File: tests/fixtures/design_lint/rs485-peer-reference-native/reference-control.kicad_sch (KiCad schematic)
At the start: 4 parts, among them J1 Synthetic RS-485 endpoint, J2 Synthetic RS-485 endpoint, J3 Synthetic RS-485 endpoint, U1 Synthetic RS-485 transceiver

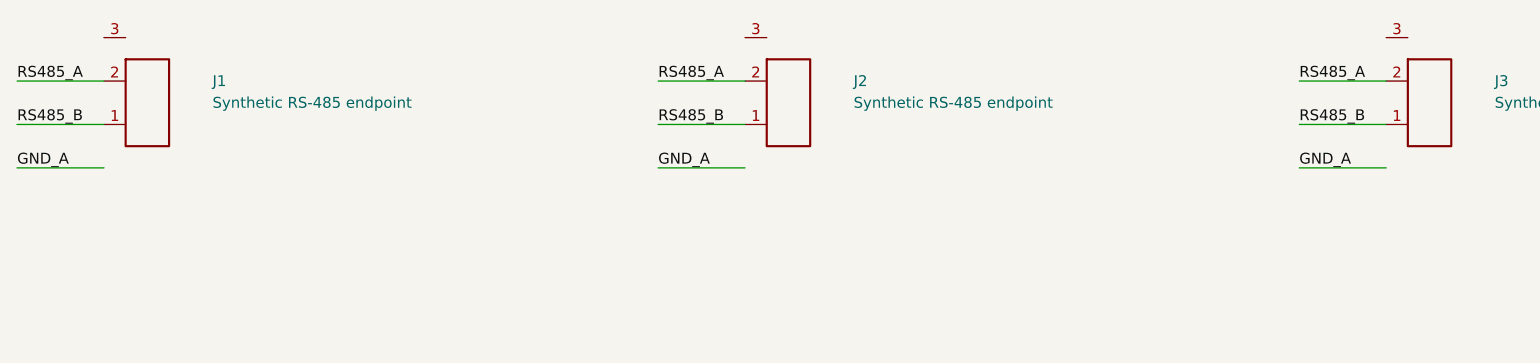
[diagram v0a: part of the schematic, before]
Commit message: Fix RS-485 native fixture gate
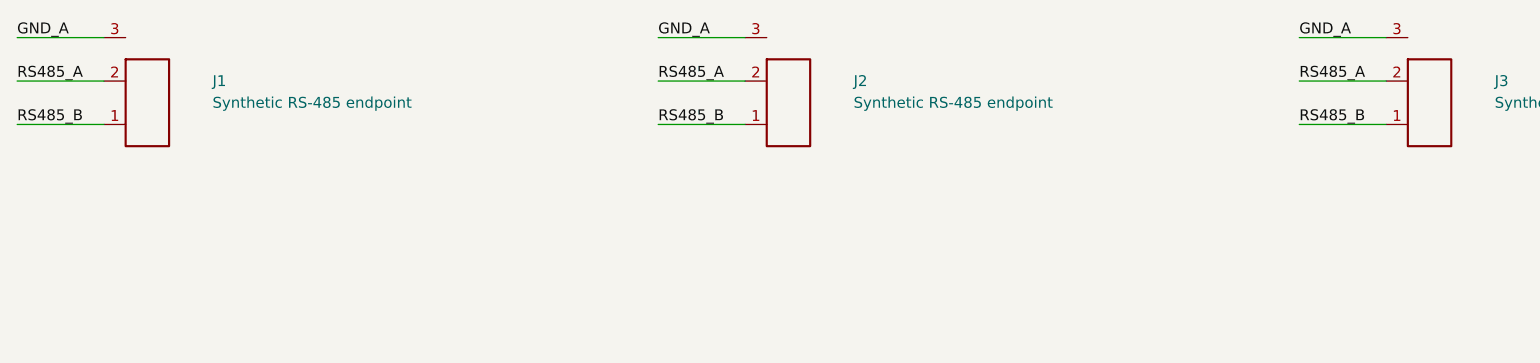
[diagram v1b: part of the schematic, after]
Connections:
- net GND_A: now also J1.3 (REF), J2.3 (REF), J3.3 (REF)
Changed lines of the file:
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@@
     (effects (font (size 1.27 1.27)) (justify left bottom))
 )
-  (wire (pts (xy 59.92 77.62) (xy 49.76 77.62))
+  (wire (pts (xy 59.92 62.38) (xy 49.76 62.38))
     (stroke (width 0) (type default))
 )
-  (label "GND_A" (at 49.76 77.62 0)
+  (label "GND_A" (at 49.76 62.38 0)
     (effects (font (size 1.27 1.27)) (justify left bottom))
 )
@@
     (effects (font (size 1.27 1.27)) (justify left bottom))
 )
-  (wire (pts (xy 134.92 77.62) (xy 124.76 77.62))
+  (wire (pts (xy 134.92 62.38) (xy 124.76 62.38))
     (stroke (width 0) (type default))
 )
-  (label "GND_A" (at 124.76 77.62 0)
+  (label "GND_A" (at 124.76 62.38 0)
     (effects (font (size 1.27 1.27)) (justify left bottom))
 )
@@
     (effects (font (size 1.27 1.27)) (justify left bottom))
 )
-  (wire (pts (xy 209.92 77.62) (xy 199.76 77.62))
+  (wire (pts (xy 209.92 62.38) (xy 199.76 62.38))
     (stroke (width 0) (type default))
 )
-  (label "GND_A" (at 199.76 77.62 0)
+  (label "GND_A" (at 199.76 62.38 0)
     (effects (font (size 1.27 1.27)) (justify left bottom))
 )

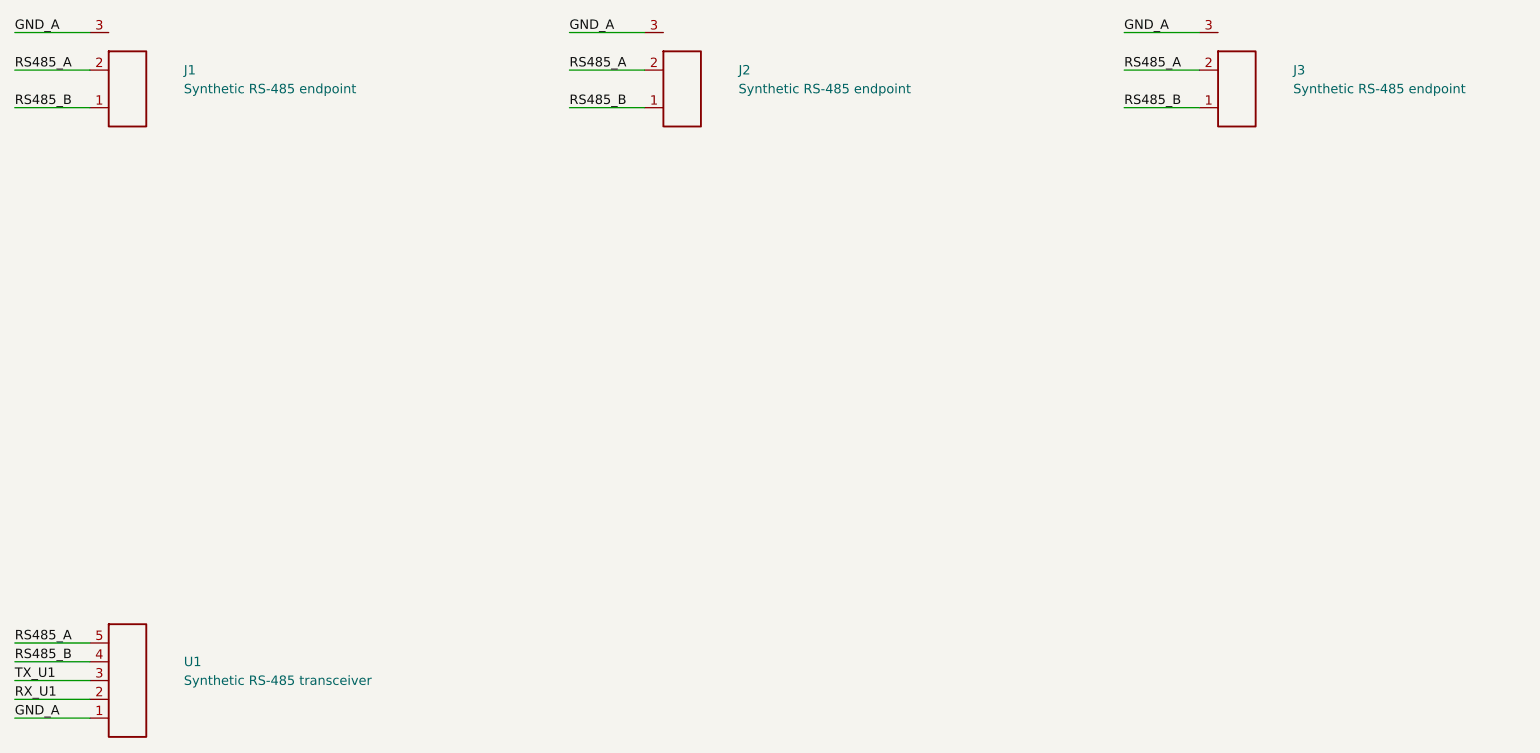
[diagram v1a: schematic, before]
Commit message: Align RS-485 fixture pins to native netlist
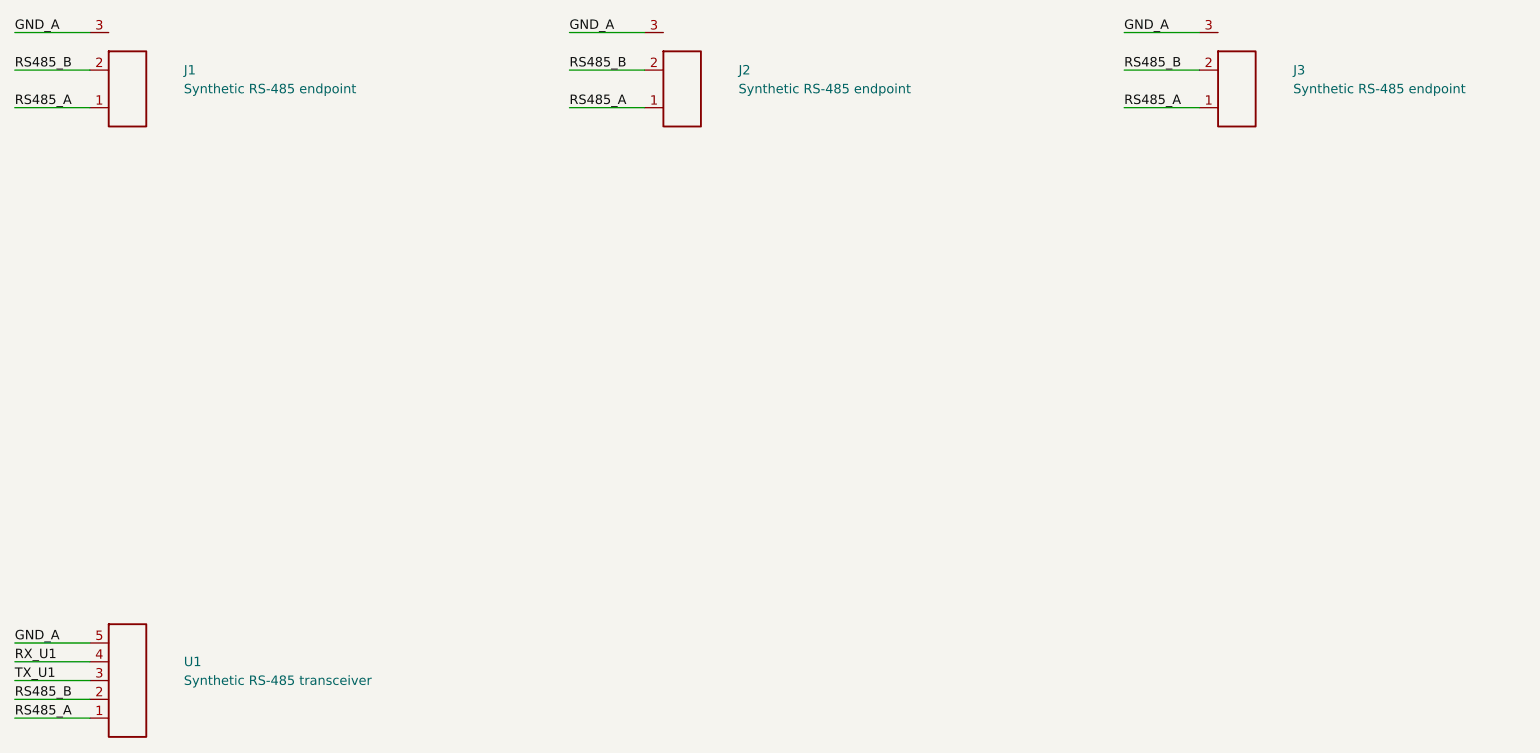
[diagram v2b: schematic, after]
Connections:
- net GND_A: now also U1.5 (REF); no longer U1.1 (A)
- net RS485_A: now also J1.1 (A), J2.1 (A), J3.1 (A), U1.1 (A); no longer J1.2 (B), J2.2 (B), J3.2 (B), U1.5 (REF)
- net RS485_B: now also J1.2 (B), J2.2 (B), J3.2 (B), U1.2 (B); no longer J1.1 (A), J2.1 (A), J3.1 (A), U1.4 (RO)
- net RX_U1: now also U1.4 (RO); no longer U1.2 (B)
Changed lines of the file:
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@@
     (stroke (width 0) (type default))
 )
-  (label "RS485_A" (at 49.76 67.46 0)
+  (label "RS485_B" (at 49.76 67.46 0)
     (effects (font (size 1.27 1.27)) (justify left bottom))
 )
@@
     (stroke (width 0) (type default))
 )
-  (label "RS485_B" (at 49.76 72.54 0)
+  (label "RS485_A" (at 49.76 72.54 0)
     (effects (font (size 1.27 1.27)) (justify left bottom))
 )
@@
     (stroke (width 0) (type default))
 )
-  (label "RS485_A" (at 124.76 67.46 0)
+  (label "RS485_B" (at 124.76 67.46 0)
     (effects (font (size 1.27 1.27)) (justify left bottom))
 )
@@
     (stroke (width 0) (type default))
 )
-  (label "RS485_B" (at 124.76 72.54 0)
+  (label "RS485_A" (at 124.76 72.54 0)
     (effects (font (size 1.27 1.27)) (justify left bottom))
 )
@@
     (stroke (width 0) (type default))
 )
-  (label "RS485_A" (at 199.76 67.46 0)
+  (label "RS485_B" (at 199.76 67.46 0)
     (effects (font (size 1.27 1.27)) (justify left bottom))
 )
@@
     (stroke (width 0) (type default))
 )
-  (label "RS485_B" (at 199.76 72.54 0)
+  (label "RS485_A" (at 199.76 72.54 0)
     (effects (font (size 1.27 1.27)) (justify left bottom))
 )
@@
     (stroke (width 0) (type default))
 )
-  (label "RS485_A" (at 49.76 144.92 0)
+  (label "GND_A" (at 49.76 144.92 0)
     (effects (font (size 1.27 1.27)) (justify left bottom))
 )
@@
     (stroke (width 0) (type default))
 )
-  (label "RS485_B" (at 49.76 147.46 0)
+  (label "RX_U1" (at 49.76 147.46 0)
     (effects (font (size 1.27 1.27)) (justify left bottom))
 )
@@
     (stroke (width 0) (type default))
 )
-  (label "RX_U1" (at 49.76 152.54 0)
+  (label "RS485_B" (at 49.76 152.54 0)
     (effects (font (size 1.27 1.27)) (justify left bottom))
 )
@@
     (stroke (width 0) (type default))
 )
-  (label "GND_A" (at 49.76 155.08 0)
+  (label "RS485_A" (at 49.76 155.08 0)
     (effects (font (size 1.27 1.27)) (justify left bottom))
 )
